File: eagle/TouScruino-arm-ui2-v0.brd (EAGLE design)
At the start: 63.5 x 72.4 mm, 45 parts, among them IC1 LMV321M5, Q2 MMBT2222A, U3 MIC5209-3.3YS, U4 MCP73831

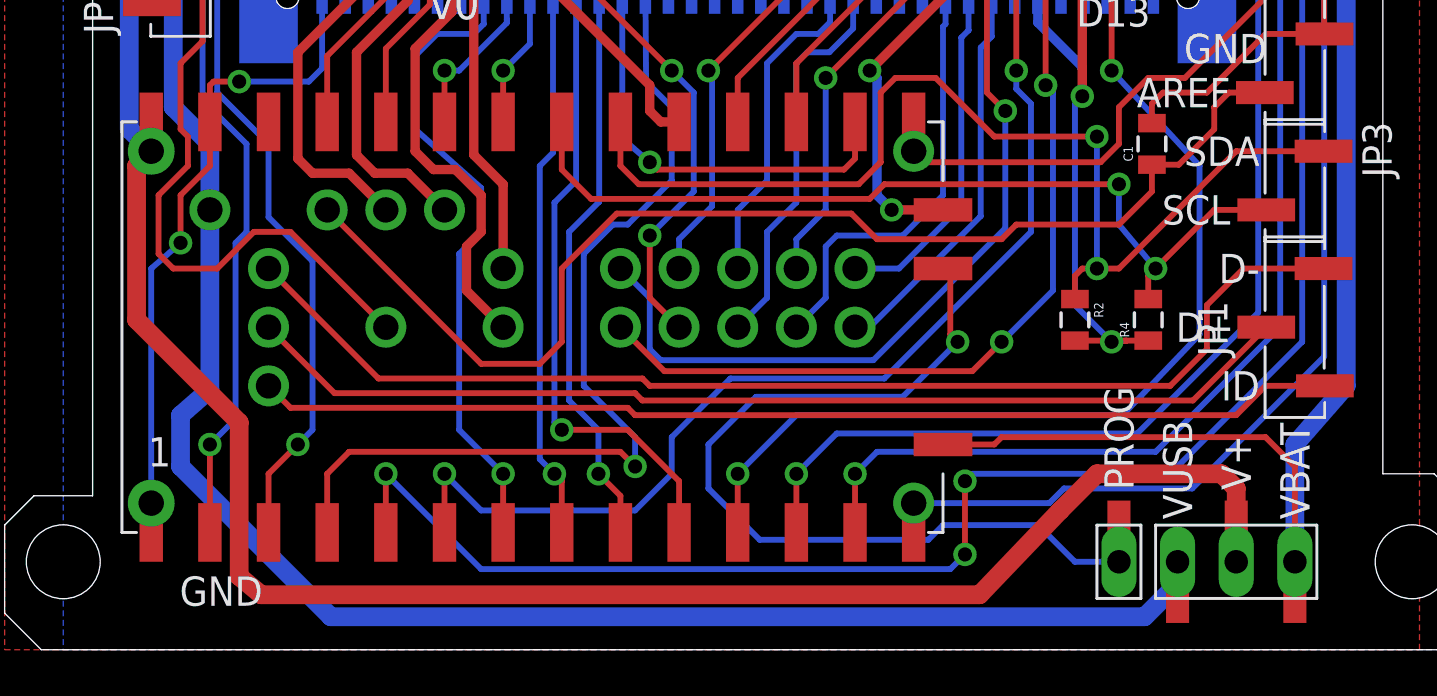
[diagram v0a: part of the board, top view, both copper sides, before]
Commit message: 
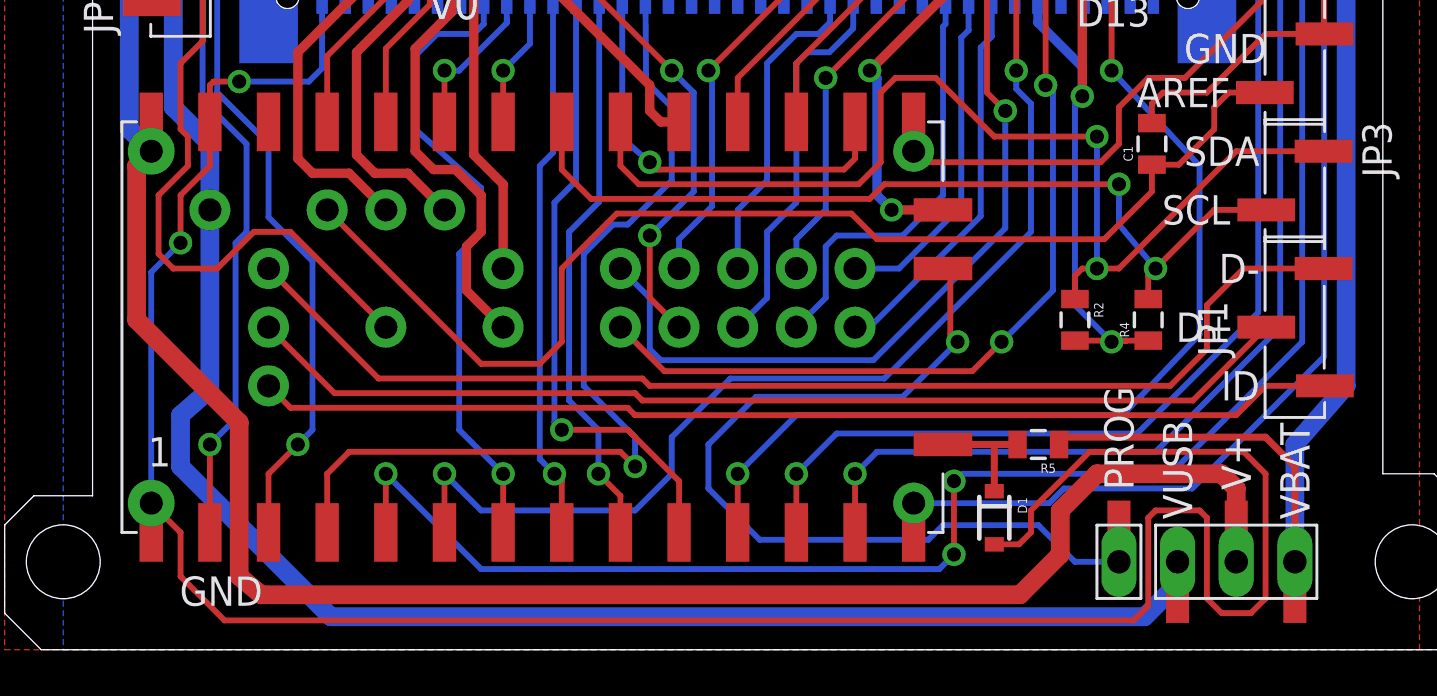
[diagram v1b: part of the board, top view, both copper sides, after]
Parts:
- added D1: 2V4, SparkFun:SOD-323
- added R5: 100k, SparkFun:0805
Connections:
- new net VBAT-: D1.1, R5.2, U$4.29
- net GND: now also D1.2
- net VBAT: now also R5.1; no longer U$4.29
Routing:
- net GND: track 342.6 -> 422.2 mm
- net VBAT-: track 0.00 -> 5.42 mm
- net VBAT: track 98.2 -> 93.7 mm
- net V+: track 127.3 -> 128.3 mm
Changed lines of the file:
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@@
 <layer number="220" name="220bmp" color="21" fill="1" visible="no" active="no"/>
 <layer number="221" name="221bmp" color="22" fill="1" visible="no" active="no"/>
+<layer number="222" name="222bmp" color="23" fill="1" visible="no" active="no"/>
 <layer number="223" name="223bmp" color="24" fill="1" visible="no" active="no"/>
 <layer number="224" name="224bmp" color="25" fill="1" visible="no" active="no"/>
@@
 <element name="C15" library="SparkFun" package="0805" value="0.1uF" x="22.225" y="67.945" rot="R270"/>
 <element name="JP8" library="wibauxl" package="1X01_SMD" value="CHARGE" x="55.88" y="66.04" rot="R90"/>
+<element name="D1" library="SparkFun" package="SOD-323" value="2V4" x="42.8625" y="5.715" rot="R270"/>
+<element name="R5" library="SparkFun" package="0805" value="100k" x="44.7675" y="8.89" rot="R180"/>
 </elements>
 <signals>
@@
 <via x="31.75" y="33.655" extent="1-16" drill="0.6096"/>
 <via x="31.75" y="37.465" extent="1-16" drill="0.6096"/>
-<wire x1="6.35" y1="6.35" x2="6.35" y2="16.51" width="0.254" layer="16"/>
-<wire x1="6.35" y1="16.51" x2="7.62" y2="17.62125" width="0.254" layer="16"/>
+<wire x1="6.35" y1="6.35" x2="6.35" y2="16.35125" width="0.254" layer="16"/>
+<wire x1="6.35" y1="16.35125" x2="7.62" y2="17.62125" width="0.254" layer="16"/>
 <wire x1="7.62" y1="17.62125" x2="7.62" y2="19.685" width="0.254" layer="1"/>
 <wire x1="7.62" y1="19.685" x2="8.89" y2="20.955" width="0.254" layer="1"/>
@@
 <via x="6.0325" y="58.42" extent="1-16" drill="0.6096"/>
 <via x="6.0325" y="63.5" extent="1-16" drill="0.6096"/>
-<wire x1="13.17625" y1="24.60625" x2="10.16" y2="24.60625" width="0.254" layer="16"/>
 <contactref element="AVRISP" pad="6"/>
 <contactref element="AVRISP" pad="6"/>
+<wire x1="13.17625" y1="24.60625" x2="10.16" y2="24.60625" width="0.254" layer="16"/>
 <wire x1="30.48" y1="67.5475" x2="30.48" y2="65.405" width="0.254" layer="1"/>
 <wire x1="30.48" y1="65.405" x2="31.75" y2="64.135" width="0.254" layer="1"/>
@@
 <wire x1="21.325" y1="66.7275" x2="19.3675" y2="64.77" width="0.254" layer="1"/>
 <wire x1="19.3675" y1="64.77" x2="18.0975" y2="64.77" width="0.254" layer="1"/>
+<contactref element="D1" pad="2"/>
+<wire x1="44.45" y1="6.0325" x2="46.99" y2="8.5725" width="0.254" layer="1"/>
+<wire x1="46.99" y1="8.5725" x2="53.6575" y2="8.5725" width="0.254" layer="1"/>
+<wire x1="53.6575" y1="8.5725" x2="54.61" y2="7.62" width="0.254" layer="1"/>
+<wire x1="54.61" y1="7.62" x2="54.61" y2="2.2225" width="0.254" layer="1"/>
+<wire x1="54.61" y1="2.2225" x2="53.975" y2="1.5875" width="0.254" layer="1"/>
+<wire x1="53.975" y1="1.5875" x2="52.705" y2="1.5875" width="0.254" layer="1"/>
+<wire x1="52.705" y1="1.5875" x2="52.07" y2="2.2225" width="0.254" layer="1"/>
+<wire x1="52.07" y1="2.2225" x2="52.07" y2="5.715" width="0.254" layer="1"/>
+<wire x1="52.07" y1="5.715" x2="51.7525" y2="6.0325" width="0.254" layer="1"/>
+<wire x1="51.7525" y1="6.0325" x2="49.8475" y2="6.0325" width="0.254" layer="1"/>
+<wire x1="49.8475" y1="6.0325" x2="49.53" y2="5.715" width="0.254" layer="1"/>
+<wire x1="49.53" y1="5.715" x2="49.53" y2="1.905" width="0.254" layer="1"/>
+<wire x1="49.53" y1="1.905" x2="48.895" y2="1.27" width="0.254" layer="1"/>
+<wire x1="48.895" y1="1.27" x2="9.525" y2="1.27" width="0.254" layer="1"/>
+<wire x1="9.525" y1="1.27" x2="7.62" y2="3.175" width="0.254" layer="1"/>
+<wire x1="7.62" y1="3.175" x2="7.62" y2="5.08" width="0.254" layer="1"/>
+<wire x1="7.62" y1="5.08" x2="6.35" y2="6.35" width="0.254" layer="1"/>
+<wire x1="42.8625" y1="4.565" x2="43.935" y2="4.565" width="0.254" layer="1"/>
+<wire x1="43.935" y1="4.565" x2="44.45" y2="5.08" width="0.254" layer="1"/>
+<wire x1="44.45" y1="5.08" x2="44.45" y2="6.0325" width="0.254" layer="1"/>
 </signal>
 <signal name="AREF">
@@
 <wire x1="26.51125" y1="18.89125" x2="36.67125" y2="18.89125" width="0.254" layer="1"/>
 <wire x1="36.67125" y1="18.89125" x2="37.7825" y2="17.78" width="0.254" layer="1"/>
-<wire x1="37.7825" y1="17.78" x2="43.18" y2="17.78" width="0.254" layer="1"/>
-<wire x1="43.18" y1="17.78" x2="43.815" y2="18.415" width="0.254" layer="1"/>
-<wire x1="43.815" y1="18.415" x2="48.26" y2="18.415" width="0.254" layer="1"/>
+<wire x1="37.7825" y1="17.78" x2="47.625" y2="17.78" width="0.254" layer="1"/>
 <wire x1="53.0225" y1="24.13" x2="54.58" y2="24.13" width="0.254" layer="1"/>
 <wire x1="55.245" y1="24.13" x2="54.58" y2="24.13" width="0.254" layer="1"/>
@@
 <wire x1="52.3875" y1="22.5425" x2="52.3875" y2="23.495" width="0.254" layer="1"/>
 <wire x1="52.3875" y1="23.495" x2="53.0225" y2="24.13" width="0.254" layer="1"/>
-<wire x1="48.26" y1="18.415" x2="49.68875" y2="19.84375" width="0.254" layer="1"/>
+<wire x1="47.625" y1="17.78" x2="49.68875" y2="19.84375" width="0.254" layer="1"/>
 <wire x1="49.68875" y1="21.0075" x2="49.68875" y2="19.84375" width="0.254" layer="1"/>
 </signal>
@@
 <contactref element="C8" pad="2"/>
 <contactref element="JP2" pad="2"/>
-<contactref element="U$4" pad="29"/>
 <wire x1="55.88" y1="8.89" x2="58.1025" y2="11.43" width="0.8128" layer="16"/>
 <wire x1="58.1025" y1="11.43" x2="58.1025" y2="55.245" width="0.8128" layer="16"/>
@@
 <contactref element="JP5" pad="3"/>
 <wire x1="55.88" y1="8.89" x2="55.88" y2="3.81" width="0.8128" layer="16"/>
-<wire x1="40.64" y1="8.89" x2="42.8625" y2="8.89" width="0.254" layer="1"/>
-<wire x1="42.8625" y1="8.89" x2="43.18" y2="9.2075" width="0.254" layer="1"/>
-<wire x1="43.18" y1="9.2075" x2="54.61" y2="9.2075" width="0.254" layer="1"/>
-<wire x1="54.61" y1="9.2075" x2="55.88" y2="7.9375" width="0.254" layer="1"/>
-<wire x1="55.88" y1="7.9375" x2="55.88" y2="3.81" width="0.254" layer="1"/>
 <wire x1="54.2925" y1="59.055" x2="44.45" y2="59.055" width="0.8128" layer="16"/>
 <wire x1="44.45" y1="59.055" x2="42.8625" y2="59.055" width="0.8128" layer="1"/>
@@
 <wire x1="42.96875" y1="55.88" x2="42.96875" y2="59.32" width="1.016" layer="1"/>
 <wire x1="42.96875" y1="59.32" x2="42.8625" y2="59.69" width="0.8128" layer="1"/>
+<wire x1="55.88" y1="3.81" x2="55.88" y2="7.9375" width="0.3048" layer="1"/>
+<wire x1="55.88" y1="7.9375" x2="54.61" y2="9.2075" width="0.3048" layer="1"/>
+<wire x1="54.61" y1="9.2075" x2="45.72" y2="9.2075" width="0.3048" layer="1"/>
+<contactref element="R5" pad="1"/>
+<wire x1="45.72" y1="9.2075" x2="45.56125" y2="8.73125" width="0.3048" layer="1"/>
+<wire x1="45.6675" y1="8.89" x2="45.56125" y2="8.73125" width="0.3048" layer="1"/>
 </signal>
 <signal name="N$4">
@@
 <wire x1="52.705" y1="7.62" x2="47.3075" y2="7.62" width="0.8128" layer="1"/>
 <wire x1="47.3075" y1="7.62" x2="45.72" y2="6.0325" width="0.8128" layer="1"/>
-<wire x1="45.72" y1="6.0325" x2="42.2275" y2="2.38125" width="0.8128" layer="1"/>
-<wire x1="42.2275" y1="2.38125" x2="11.1125" y2="2.38125" width="0.8128" layer="1"/>
+<wire x1="45.72" y1="6.0325" x2="45.72" y2="4.1275" width="0.8128" layer="1"/>
+<wire x1="45.72" y1="4.1275" x2="43.97375" y2="2.38125" width="0.8128" layer="1"/>
+<wire x1="43.97375" y1="2.38125" x2="11.1125" y2="2.38125" width="0.8128" layer="1"/>
 <wire x1="11.1125" y1="2.38125" x2="10.16" y2="3.175" width="0.8128" layer="1"/>
 <wire x1="10.16" y1="3.175" x2="10.16" y2="9.8425" width="0.8128" layer="1"/>
@@
 <wire x1="16.51" y1="5.08" x2="16.51" y2="7.62" width="0.254" layer="1"/>
 <wire x1="16.51" y1="7.62" x2="20.6375" y2="3.4925" width="0.254" layer="16"/>
-<wire x1="20.6375" y1="3.4925" x2="40.9575" y2="3.4925" width="0.254" layer="16"/>
-<wire x1="40.9575" y1="3.4925" x2="41.5925" y2="4.1275" width="0.254" layer="16"/>
-<wire x1="41.5925" y1="4.1275" x2="41.5925" y2="7.3025" width="0.254" layer="1"/>
-<via x="41.5925" y="7.3025" extent="1-16" drill="0.6096"/>
-<via x="41.5925" y="4.1275" extent="1-16" drill="0.6096"/>
+<wire x1="20.6375" y1="3.4925" x2="40.48125" y2="3.4925" width="0.254" layer="16"/>
+<wire x1="40.48125" y1="3.4925" x2="41.11625" y2="4.1275" width="0.254" layer="16"/>
+<wire x1="41.11625" y1="4.1275" x2="41.11625" y2="7.3025" width="0.254" layer="1"/>
+<via x="41.11625" y="7.3025" extent="1-16" drill="0.6096"/>
+<via x="41.11625" y="4.1275" extent="1-16" drill="0.6096"/>
 <via x="16.51" y="7.62" extent="1-16" drill="0.6096"/>
-<wire x1="41.5925" y1="7.3025" x2="41.91" y2="7.62" width="0.254" layer="16"/>
-<wire x1="41.91" y1="7.62" x2="50.4825" y2="7.62" width="0.254" layer="16"/>
+<wire x1="41.11625" y1="7.3025" x2="41.43375" y2="7.62" width="0.254" layer="16"/>
+<wire x1="41.43375" y1="7.62" x2="50.4825" y2="7.62" width="0.254" layer="16"/>
 <wire x1="50.4825" y1="7.62" x2="56.1975" y2="13.335" width="0.254" layer="16"/>
 <wire x1="56.1975" y1="13.335" x2="56.1975" y2="32.0675" width="0.254" layer="16"/>
@@
 <wire x1="8.89" y1="63.52" x2="8.91" y2="63.5" width="0.4064" layer="1"/>
 </signal>
+<signal name="VBAT-">
+<contactref element="U$4" pad="29"/>
+<contactref element="R5" pad="2"/>
+<contactref element="D1" pad="1"/>
+<wire x1="40.76" y1="8.77" x2="40.64" y2="8.89" width="0.3048" layer="1"/>
+<wire x1="43.8675" y1="8.89" x2="42.8625" y2="8.89" width="0.3048" layer="1"/>
+<wire x1="42.8625" y1="8.89" x2="40.64" y2="8.89" width="0.3048" layer="1"/>
+<wire x1="42.8625" y1="6.865" x2="42.8625" y2="8.89" width="0.3048" layer="1"/>
+</signal>
 </signals>
-<errors>
-</errors>
 </board>
 </drawing>
